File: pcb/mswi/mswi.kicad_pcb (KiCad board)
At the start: 2 copper layers, 140 x 72.3 mm, 164 parts, among them J301 AVR-ISP-6, J302 USART, J303 I2C, J501 RJ45, Q301 BC856, Q401 BC856, Q402 BC856, Q403 BC856, Q404 BC856, Q405 BC856, Q406 BC856, Q407 BC856, Q408 BC856, Q409 BC856, Q410 BC856, Q411 BC856, Q412 BC856, Q413 BC856, Q414 BC856, Q415 BC856, Q416 BC856, Q417 BC856, Q418 BC856, Q419 BC856, Q420 BC856, Q601 si2308cds, SW401 SW_Push, SW402 SW_Push, SW403 SW_Push, SW404 SW_Push, SW405 SW_Push, SW406 SW_Push, SW407 SW_Push, SW408 SW_Push, SW409 SW_Push, SW410 SW_Push, U201 MCP2551-I/SN, U202 MCP2515-xSO, U301 ATmega328PB-AU, U601 LM7805, Y201 16MHz, Y301 16MHz

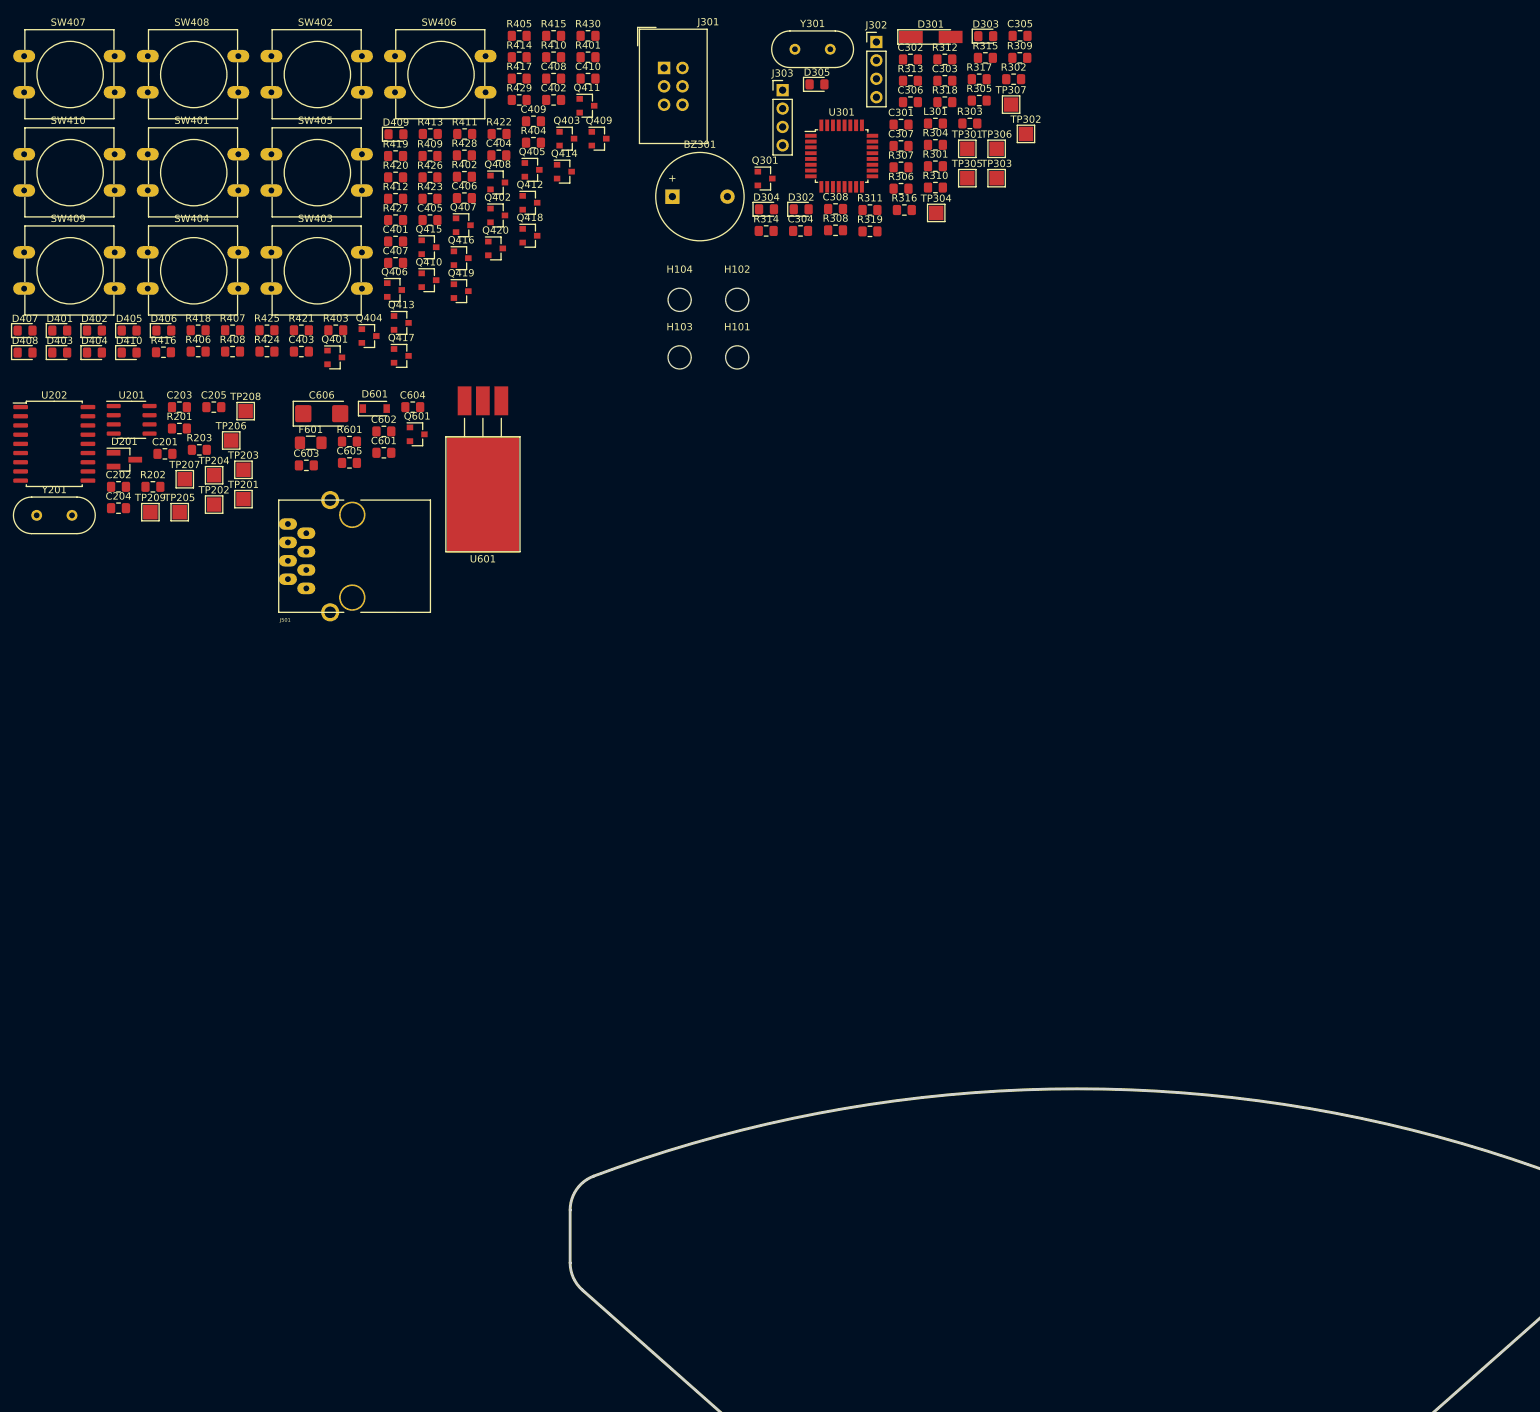
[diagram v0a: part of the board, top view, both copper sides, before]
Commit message: Switch&led interface first iteration
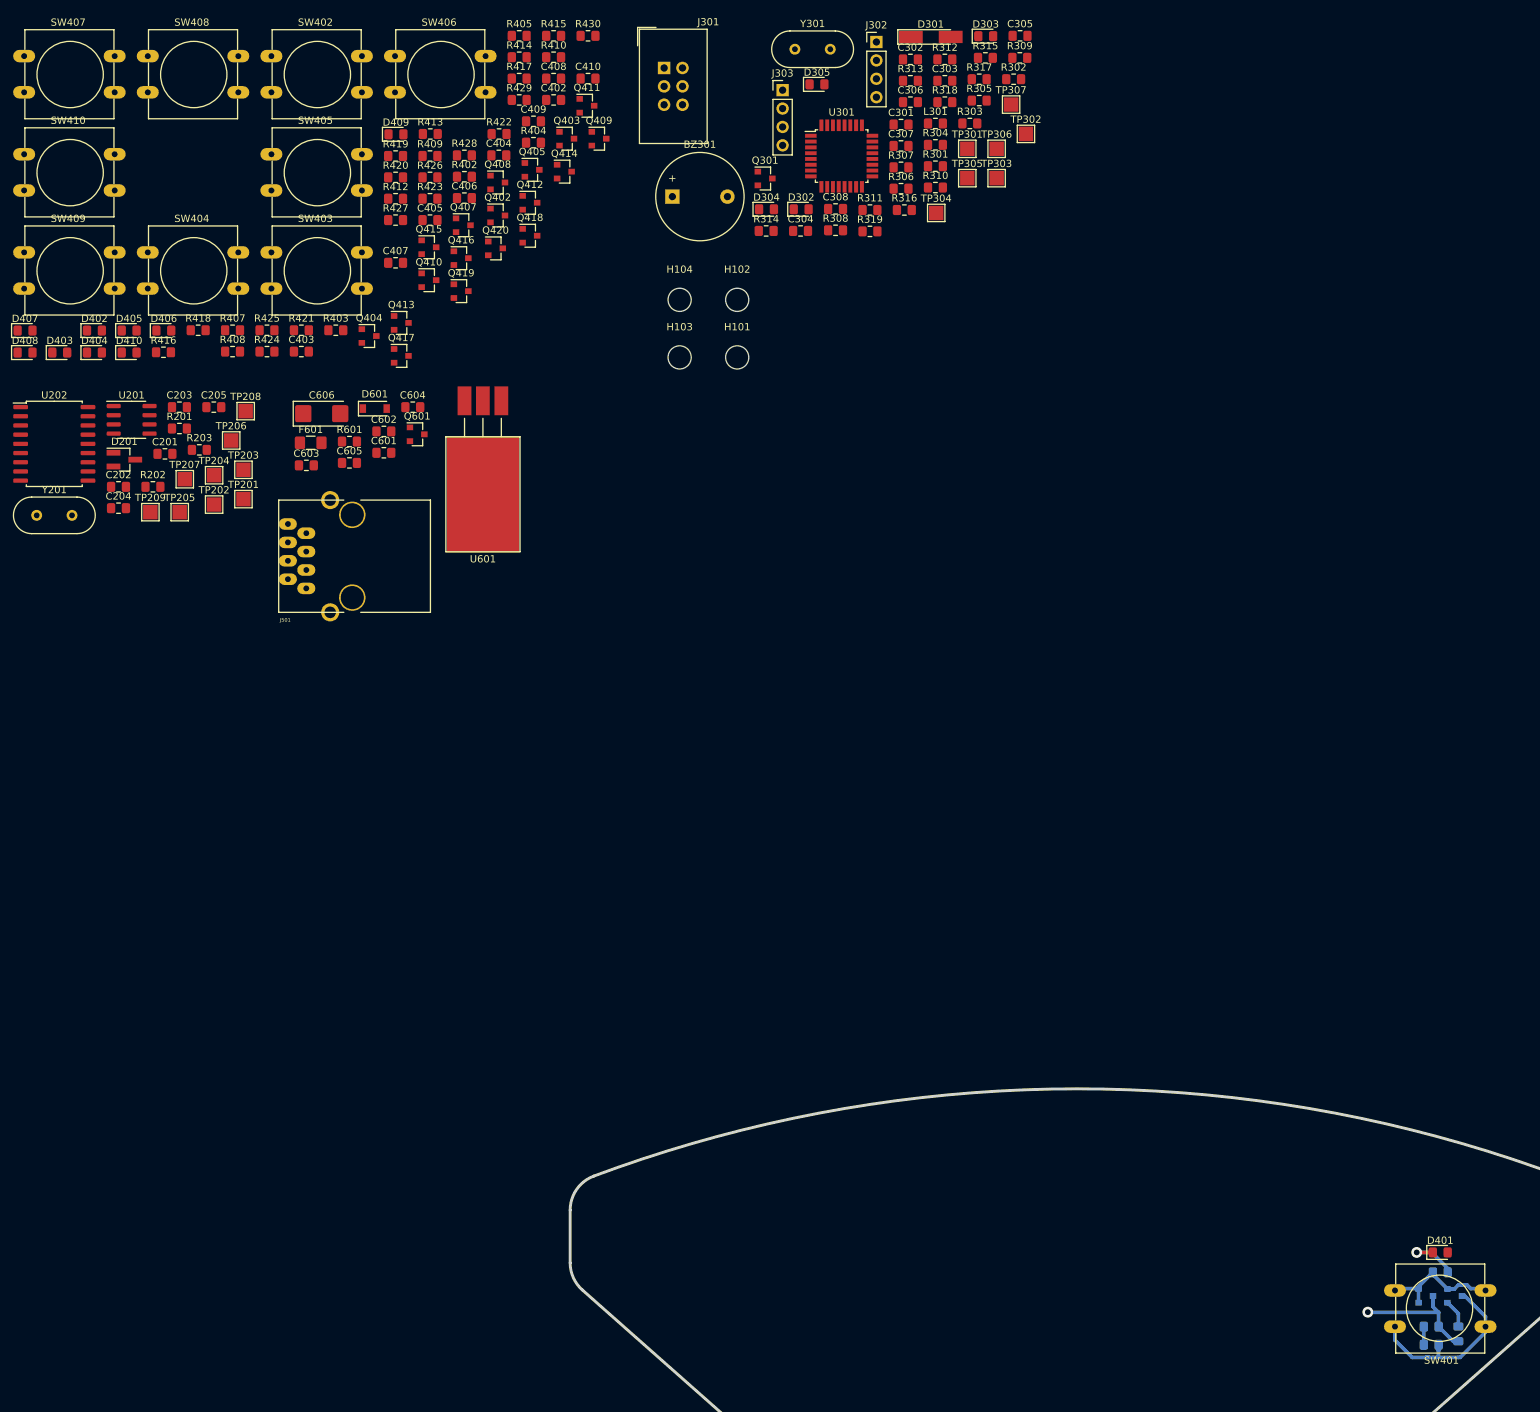
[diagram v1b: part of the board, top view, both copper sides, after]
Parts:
- C401, Q401, Q406, R401, R406, R411: moved to B.Cu
- moved SW401 245.6 mm to (201.8, 83.8), turned to 180 degrees
- moved D401 229.2 mm to (195.5, 73.5)
- moved R406 220.6 mm to (198.0, 84.8), turned to 270 degrees
- moved R411 213.9 mm to (194.2, 86.2)
- moved C401 207.1 mm to (194.2, 83.8), turned to 180 degrees
- moved R401 204.9 mm to (195.5, 76.2), turned to 180 degrees
- moved Q401 201.8 mm to (197.5, 79.5)
- moved Q406 198.9 mm to (193.5, 79.5)
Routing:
- net GND: track 0.00 -> 25.5 mm
- net /MCU/SW0: track 0.00 -> 17.9 mm, vias 0 -> 1
- net Net-(Q401-Pad2): track 0.00 -> 17.1 mm
- net Net-(D401-Pad1): track 0.00 -> 7.41 mm, vias 0 -> 1
- net Net-(Q401-Pad1): track 0.00 -> 3.90 mm
- net Net-(C401-Pad2): track 0.00 -> 2.50 mm

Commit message: Buzzer interface first iteration
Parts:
- added D306: LED_RED, LED_SMD:LED_0805_2012Metric_Pad1.15x1.40mm_HandSolder, F.Cu at (161.0, 102.5)
- added R320: 1k, Resistor_SMD:R_0805_2012Metric_Pad1.15x1.40mm_HandSolder, F.Cu at (164.8, 101.5)
- J301: footprint Connector_IDC:IDC-Header_2x03_P2.54mm_Vertical -> Connector_IDC:IDC-Header_2x03_P2.54mm_Horizontal
- Q301, R318, R319, TP306, TP307: moved to B.Cu
- moved TP307 185.1 mm to (156.0, 99.0)
- moved Q301 182.5 mm to (160.2, 98.2), turned to 270 degrees
- moved R318 179.8 mm to (161.0, 91.2), turned to 270 degrees
- moved BZ301 179.4 mm to (155.0, 94.7)
- moved TP306 171.3 mm to (156.5, 91.0)
- moved R319 167.0 mm to (158.5, 94.2), turned to 270 degrees
- moved C201 73.6 mm to (63.7, 22.0)
- moved C202 73.6 mm to (57.2, 26.5)
- moved C203 73.6 mm to (65.7, 15.5)
- moved C204 73.6 mm to (57.2, 29.5)
- moved C205 73.6 mm to (70.4, 15.5)
- moved C301 73.6 mm to (165.3, -23.5)
- moved C302 73.6 mm to (166.6, -32.5)
- moved C303 73.6 mm to (171.3, -29.5)
- moved C304 73.6 mm to (151.4, -8.80)
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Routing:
- net Net-(BZ301-Pad1): track 0.00 -> 17.1 mm, vias 0 -> 1
- net /MCU/BUZZER: track 0.00 -> 13.6 mm, vias 0 -> 1
- net +5V: track 0.00 -> 11.0 mm, vias 0 -> 1
- net GND: track 25.5 -> 35.9 mm, vias 0 -> 1
- net Net-(D306-Pad1): track 0.00 -> 2.74 mm
- net Net-(Q301-Pad1): track 0.00 -> 2.31 mm

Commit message: _
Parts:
- C402, C403, C404, C405, C406, C407, C408, C409, C410, D402, D403, D404, D405, D406, D407, D408, D409, D410, Q402, Q403, Q404, Q405, Q407, Q408, Q409, Q410, Q411, Q412, Q413, Q414, Q415, Q416, Q417, Q418, Q419, Q420, R402, R403, R404, R405, R407, R408, R409, R410, R412, R413, R414, R415, R416, R417, R418, R419, R420, R421, R422, R423, R424, R425, R426, R427, R428, R429, R430, SW404, SW405, SW407, SW409: moved to B.Cu
- J301: footprint Connector_IDC:IDC-Header_2x03_P2.54mm_Horizontal -> Connector_IDC:IDC-Header_2x03_P2.54mm_Vertical
- moved Q409 186.5 mm to (-35.1, 76.5), turned to 180 degrees
- moved C410 183.9 mm to (-33.6, 68.2), turned to 180 degrees
- moved R430 183.9 mm to (-33.6, 62.3), turned to 180 degrees
- moved Q411 183.7 mm to (-33.4, 71.9), turned to 180 degrees
- moved Q403 179.0 mm to (-30.6, 76.5), turned to 180 degrees
- moved SW407 179.0 mm to (191.5, 68.8), turned to 131.8 degrees
- moved Q414 178.4 mm to (-30.3, 81.0), turned to 180 degrees
- moved C402 176.0 mm to (-28.8, 71.1), turned to 180 degrees
- moved C408 176.0 mm to (-28.8, 68.2), turned to 180 degrees
- moved R410 176.0 mm to (-28.8, 65.2), turned to 180 degrees
- moved R415 176.0 mm to (-28.8, 62.3), turned to 180 degrees
- moved SW410 172.8 mm to (179.8, 87.8), turned to 311.8 degrees
- moved C409 171.4 mm to (-26.0, 74.1), turned to 180 degrees
- moved R404 171.4 mm to (-26.0, 77.0), turned to 180 degrees
- moved Q405 171.1 mm to (-25.9, 80.8), turned to 180 degrees
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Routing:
- net /MCU/SW0: track 17.9 -> 19.3 mm
- net Net-(Q401-Pad2): track 17.1 -> 18.2 mm
- net Net-(D401-Pad1): track 7.41 -> 8.23 mm
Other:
- board text added: "TODO: [_] Adapt Rules to Fabrication Method [x] ISP: Change to VERTICAL Version [_] OLED: Footprint & 3D [_] SW: 3D [_] RJ45: 3D [_] Fuse: 3D [x] PCB Geometry [_] Add zenitesolar and designer identification [_] Add opensource hardware symbol [_] Define the switches position -> paper prototype"
- board text removed: "TODO: [x] ISP: Change to VERTICAL Version [_] OLED: Footprint & 3D [_] SW: 3D [_] RJ45: 3D [_] Fuse: 3D [x] PCB Geometry [_] Add zenitesolar and designer identification [_] Add opensource hardware symbol [_] Define the switches position -> paper prototype"

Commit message: all swiches&leds interface routed
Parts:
- D402, D403, D404, D405, D406, D407, D408, D409, D410, SW404, SW407: moved to F.Cu
- moved R417 218.7 mm to (194.1, 83.5), turned to 270 degrees
- moved Q412 216.4 mm to (190.8, 87.8), turned to 270 degrees
- moved Q409 211.6 mm to (176.3, 83.8), turned to 270 degrees
- moved R422 207.3 mm to (185.6, 88.8)
- moved R404 205.7 mm to (179.6, 83.5), turned to 270 degrees
- moved Q417 199.9 mm to (190.8, 83.8), turned to 270 degrees
- moved R414 194.6 mm to (169.6, 84.5), turned to 270 degrees
- moved C407 193.8 mm to (186.6, 84.5), turned to 270 degrees
- moved C404 193.4 mm to (172.1, 84.5), turned to 270 degrees
- moved Q403 192.8 mm to (161.8, 87.8), turned to 270 degrees
- moved R427 191.1 mm to (184.1, 84.5), turned to 270 degrees
- moved R409 183.1 mm to (171.1, 88.8)
- moved Q408 182.9 mm to (161.8, 83.8), turned to 270 degrees
- moved Q404 180.4 mm to (176.3, 87.8), turned to 270 degrees
- moved Q418 172.9 mm to (147.2, 83.8), turned to 270 degrees
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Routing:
- net GND: track 35.9 -> 344.5 mm, vias 1 -> 11
- net (no net): track 0.00 -> 238.3 mm, vias 0 -> 9
- net Net-(Q403-Pad2): track 0.00 -> 17.2 mm
- net Net-(Q405-Pad2): track 0.00 -> 17.2 mm
- net Net-(Q402-Pad2): track 0.00 -> 17.2 mm
- net Net-(Q415-Pad2): track 0.00 -> 17.2 mm
- net Net-(Q414-Pad2): track 0.00 -> 17.2 mm
- net Net-(Q413-Pad2): track 0.00 -> 17.2 mm
- net Net-(Q411-Pad2): track 0.00 -> 17.2 mm
- net Net-(D403-Pad1): track 0.00 -> 9.51 mm, vias 0 -> 1
- net Net-(D406-Pad1): track 0.00 -> 9.51 mm, vias 0 -> 1
- net Net-(D402-Pad1): track 0.00 -> 9.51 mm, vias 0 -> 1
- net Net-(D410-Pad1): track 0.00 -> 9.51 mm, vias 0 -> 1
- net Net-(D408-Pad1): track 0.00 -> 9.51 mm, vias 0 -> 1
- net Net-(D407-Pad1): track 0.00 -> 9.51 mm, vias 0 -> 1
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
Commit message: input and power supply routed
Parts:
- added D602: 400W 24VDC, Diode_SMD:D_SMA, B.Cu at (37.6, -12.8)
- C601, C602, C603, C604, C605, C606, D601, F601, Q601, R601, U601: moved to B.Cu
- moved SW407 264.9 mm to (434.6, 127.6)
- moved Q404 250.5 mm to (424.4, 123.4)
- moved Q409 250.5 mm to (424.4, 119.4)
- moved Q412 250.5 mm to (438.9, 123.4)
- moved Q417 250.5 mm to (438.9, 119.4)
- moved R404 250.5 mm to (427.6, 119.1)
- moved R409 250.5 mm to (419.1, 124.4)
- moved R417 250.5 mm to (442.1, 119.1)
- moved R422 250.5 mm to (433.6, 124.4)
- moved C401 250.5 mm to (361.9, 120.1)
- moved C402 250.5 mm to (332.8, 119.9), turned to 90 degrees
- moved C403 250.5 mm to (405.5, 120.1), turned to 90 degrees
- moved C404 250.5 mm to (420.1, 120.1), turned to 90 degrees
- moved C405 250.5 mm to (303.9, 120.1), turned to 90 degrees
- moved C406 250.5 mm to (347.3, 120.1), turned to 90 degrees
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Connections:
- net Net-(C601-Pad1) renamed /POWER SUPPLY/+18V
- U601 pad : (no net) -> GND
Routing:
- net (no net): track 238.3 -> 0.00 mm, vias 9 -> 0
- net /CANBUS CONN/CAN_GND: track 0.00 -> 26.4 mm
- net /MCU/SW6: track 0.00 -> 20.1 mm, vias 0 -> 1
- net /MCU/SW2: track 0.00 -> 20.1 mm, vias 0 -> 1
- net /MCU/SW1: track 0.00 -> 20.1 mm, vias 0 -> 1
- net /MCU/SW5: track 0.00 -> 20.1 mm, vias 0 -> 1
- net /MCU/SW8: track 0.00 -> 20.1 mm, vias 0 -> 1
- net /MCU/SW9: track 0.00 -> 20.1 mm, vias 0 -> 1
- net /MCU/SW7: track 0.00 -> 20.1 mm, vias 0 -> 1
- net /MCU/SW3: track 0.00 -> 20.1 mm, vias 0 -> 1
- net /MCU/SW4: track 0.00 -> 20.1 mm, vias 0 -> 1
- net Net-(Q412-Pad2): track 0.00 -> 17.2 mm
- net Net-(Q404-Pad2): track 0.00 -> 17.2 mm
- net /POWER SUPPLY/+18V: track 0.00 -> 14.3 mm, vias 0 -> 1
- net Net-(D601-Pad1): track 0.00 -> 9.94 mm
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
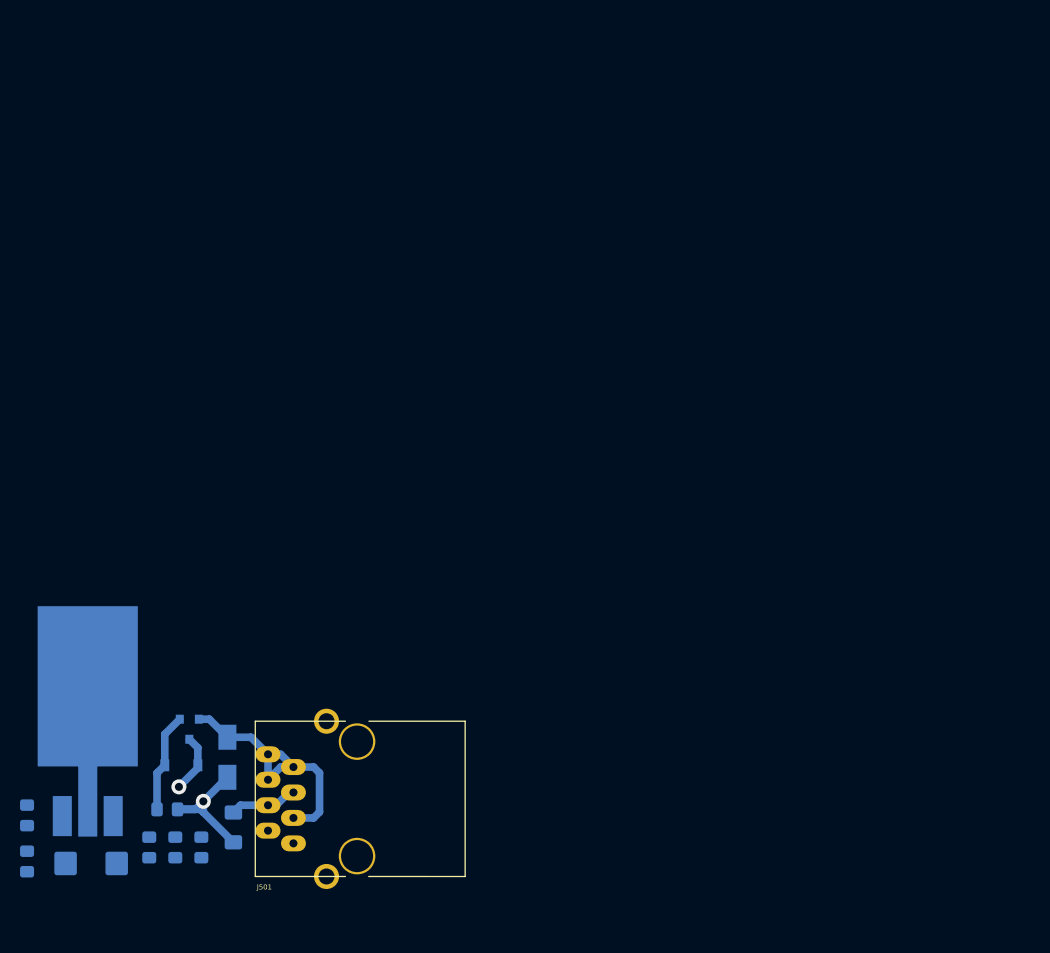
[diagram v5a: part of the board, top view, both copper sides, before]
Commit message: pwr sup. rounted with new can connector
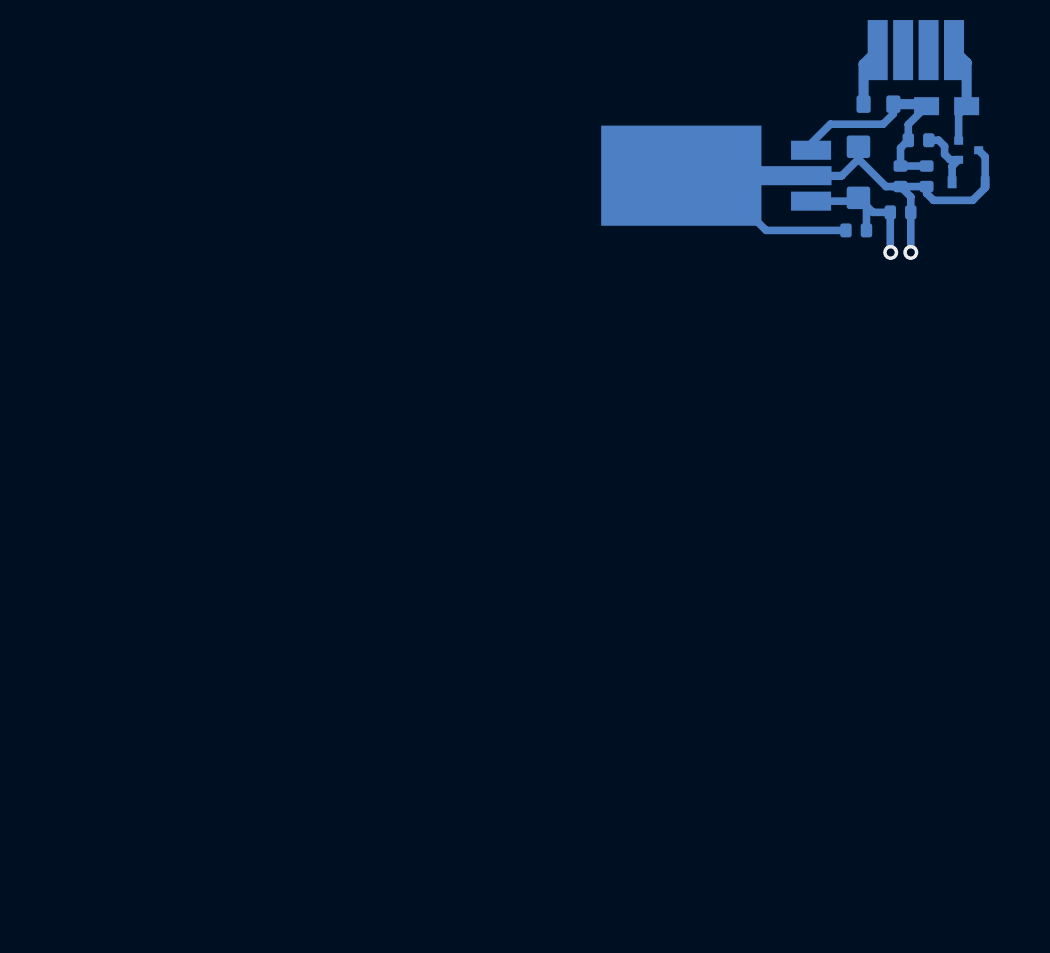
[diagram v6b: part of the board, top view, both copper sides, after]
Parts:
- removed C602: 100nF, Capacitor_SMD:C_0805_2012Metric_Pad1.15x1.40mm_HandSolder
- J501: value RJ45 -> Conn_01x04_Male; footprint KicadZeniteSolarLibrary18:RJ45_YH59_01 -> Connector_PinHeader_2.54mm:PinHeader_1x04_P2.54mm_Horizontal; moved to B.Cu
- moved C604 108.6 mm to (104.8, -67.2), turned to 0 degrees
- moved J501 104.9 mm to (110.1, -85.8)
- moved C606 103.1 mm to (100.6, -71.2), turned to 90 degrees
- moved C605 101.3 mm to (100.4, -65.4), turned to 180 degrees
- moved C601 100.6 mm to (104.8, -70.8)
- moved R601 100.4 mm to (106.6, -74.4), turned to 0 degrees
- moved C603 98.6 mm to (107.4, -70.8)
- moved D601 97.8 mm to (111.6, -70.2)
- moved Q601 96.9 mm to (111.6, -73.4), turned to 0 degrees
- moved D602 96.9 mm to (109.4, -77.8), turned to 0 degrees
- moved F601 96.7 mm to (102.6, -78.0), turned to 0 degrees
- moved U601 94.5 mm to (94.6, -73.4), turned to 270 degrees
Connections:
- J501 pad 1: /CANBUS CONN/CAN_H -> /CANBUS CONN/CAN_GND
- J501 pad 2: /CANBUS CONN/CAN_L -> /CANBUS CONN/CAN_H
- J501 pad 3: /CANBUS CONN/CAN_GND -> /CANBUS CONN/CAN_L
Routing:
- net GND: track 352.2 -> 415.9 mm
- net /CANBUS CONN/CAN_GND: track 26.4 -> 9.90 mm
- net +5V: track 11.0 -> 27.2 mm, vias 1 -> 2
- net /POWER SUPPLY/+18V: track 14.3 -> 23.9 mm, vias 1 -> 0
- net Net-(D601-Pad1): track 9.94 -> 6.77 mm
- net /POWER SUPPLY/+18V_IN: track 7.60 -> 5.98 mm
